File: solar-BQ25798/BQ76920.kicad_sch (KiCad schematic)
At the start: 33 parts, among them Q1801 CSD17581Q3A, Q1802 CSD17581Q3A, Q1803 Q_PMOS_GSD, U2 BQ76920PW

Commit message: BQ25798 WIP
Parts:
- Q1801: renamed from Q1802; value CSD17581Q3A -> CSD17578Q3A; symbol Transistor_FET:CSD17581Q3A -> cacophony-library:CSD17578Q3A; LCSC Part C2866708 -> C205986
- Q1803: renamed from Q1801; value CSD17581Q3A -> CSD17578Q3A; symbol Transistor_FET:CSD17581Q3A -> cacophony-library:CSD17578Q3A; LCSC Part C2866708 -> C205986
- renumbered C6 to C1801, C1803 to C1802, C3 to C1803, C2 to C1804, C1 to C1805, C4 to C1806, C5 to C1807, C1801 to C1808, C1802 to C1809, C7 to C1810, C8 to C1811, C10 to C1812, C9 to C1813, D1802 to D1801, Q1803 to Q1802, R6 to R1801, R5 to R1802, R4 to R1803, R3 to R1804, R2 to R1805, R1 to R1806, R1801 to R1807, R211 to R1808, R1802 to R1809, R1803 to R1810, R7 to R1811, R1805 to R1812, R1804 to R1813, R9 to R1814, U2 to U1801

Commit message: Solar battery WIP
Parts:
- U1801: footprint cacophony-library:TSSOP-20_4.4x6.5mm_P0.65mm -> Package_SO:TSSOP-20_4.4x6.5mm_P0.65mm
- renumbered C1803 to C1801, C1810 to C1802, C1804 to C1803, C1805 to C1804, C1806 to C1805, C1813 to C1806, C1812 to C1807, C1807 to C1808, C1811 to C1809, C1801 to C1810, C1802 to C1811, C1808 to C1812, C1809 to C1813, Q1802 to Q1801, Q1801 to Q1802, R1811 to R1801, R1801 to R1802, R1802 to R1803, R1803 to R1804, R1804 to R1805, R1814 to R1806, R1805 to R1807, R1806 to R1808, R1812 to R1809, R1807 to R1810, R1809 to R1811, R1810 to R1812, R1808 to R1814
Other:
- moved on the sheet: C1801, C1802, C1803, C1804, C1805, C1806, C1807, C1808, C1809, C1810, C1811, C1812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

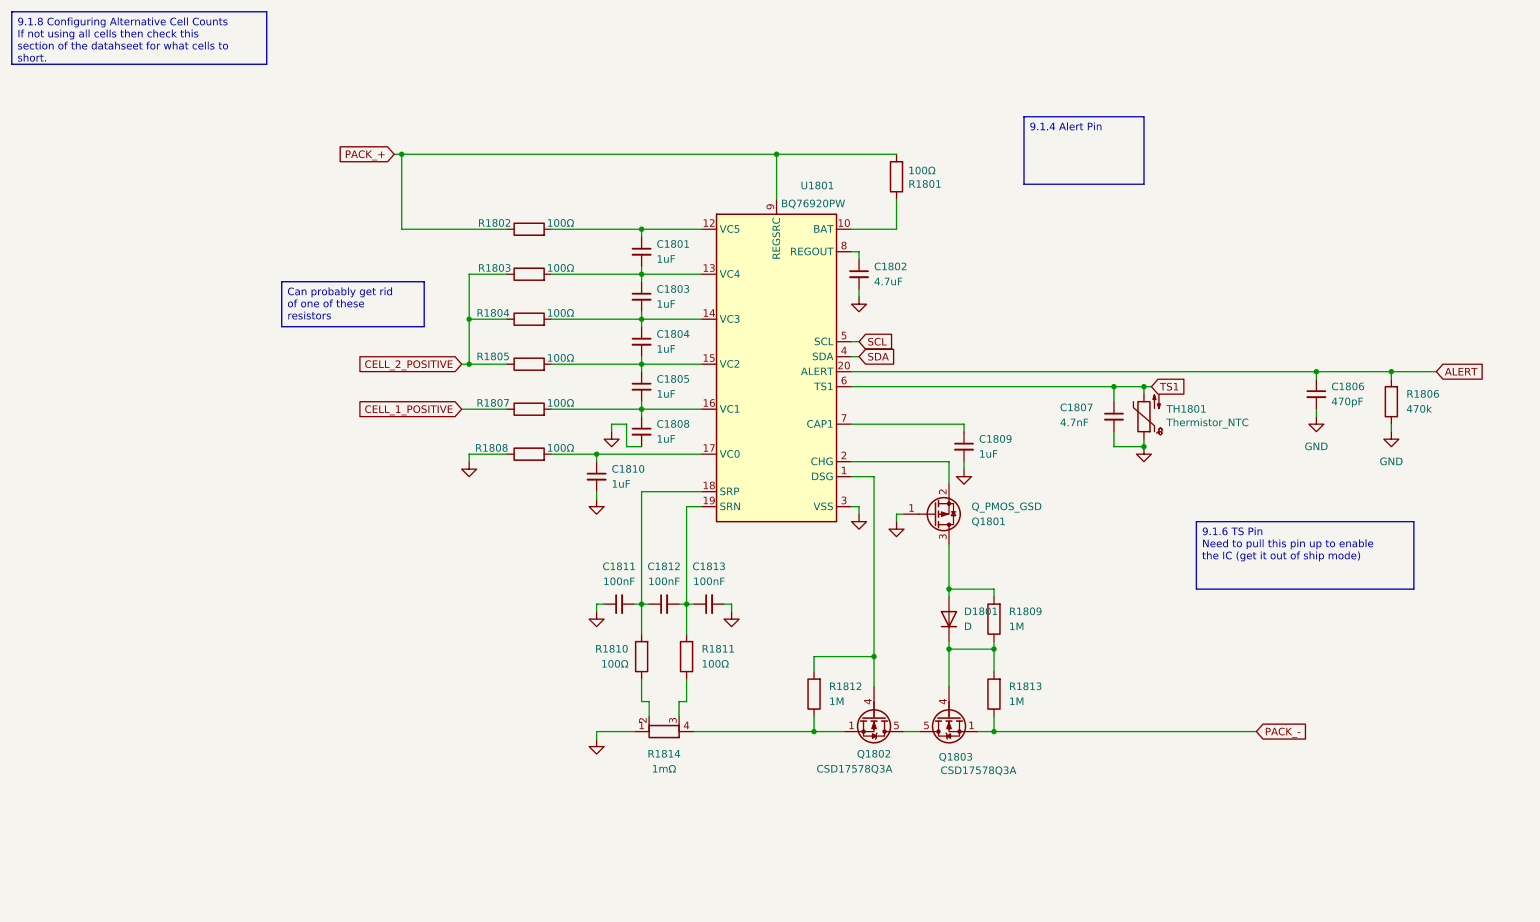
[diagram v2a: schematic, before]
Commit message: Update battery PCB
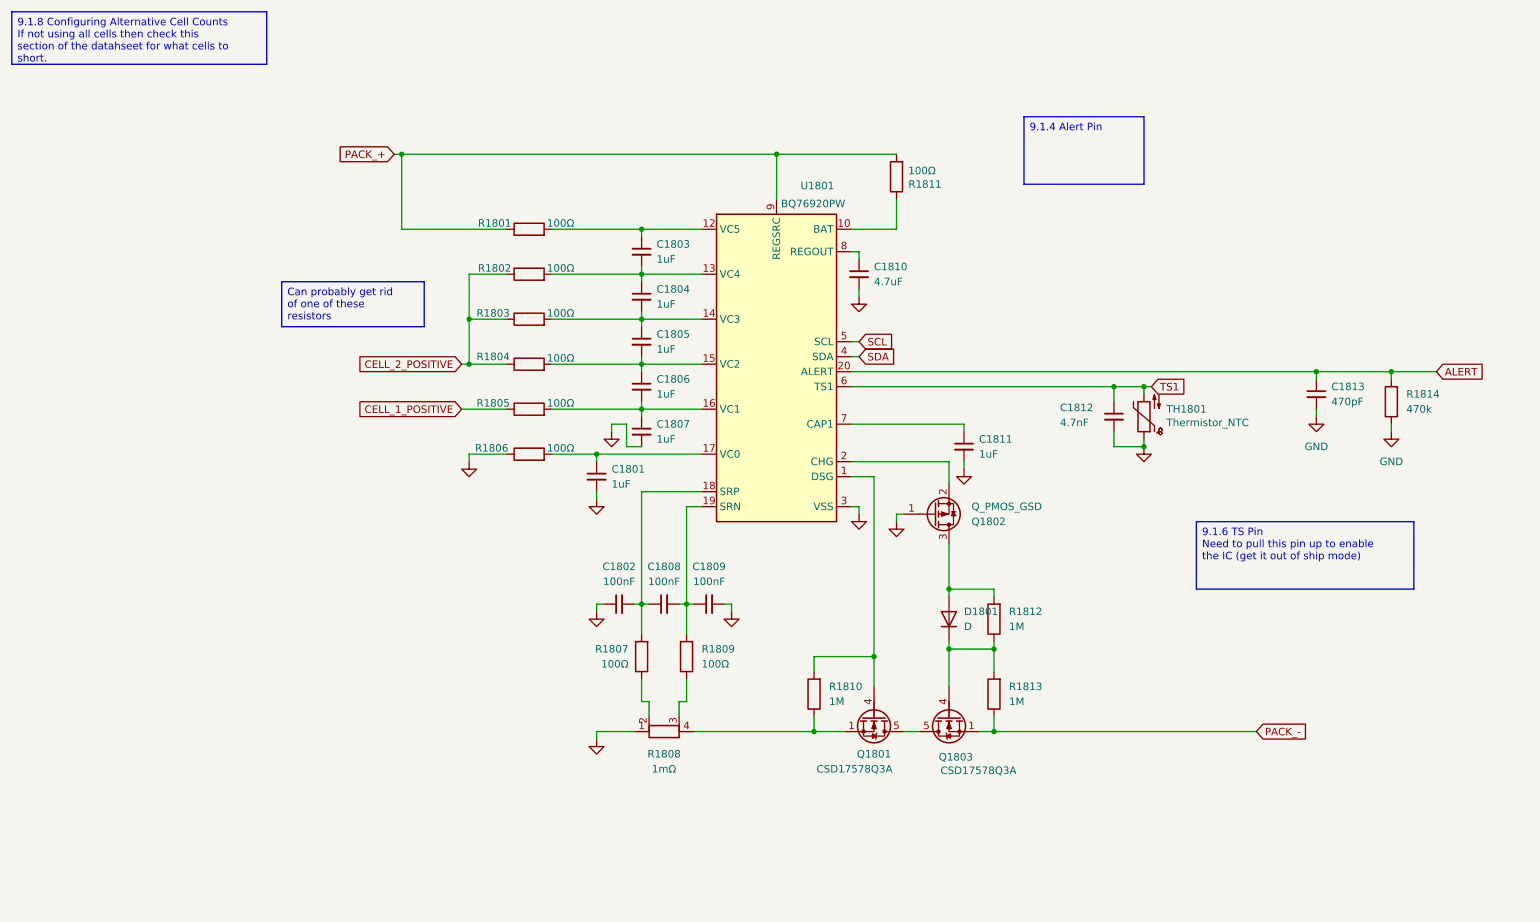
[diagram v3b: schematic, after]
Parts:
- renumbered C1810 to C1801, C1811 to C1802, C1801 to C1803, C1803 to C1804, C1804 to C1805, C1805 to C1806, C1808 to C1807, C1812 to C1808, C1813 to C1809, C1802 to C1810, C1809 to C1811, C1807 to C1812, C1806 to C1813, Q1802 to Q1801, Q1801 to Q1802, R1802 to R1801, R1803 to R1802, R1804 to R1803, R1805 to R1804, R1807 to R1805, R1808 to R1806, R1810 to R1807, R1814 to R1808, R1811 to R1809, R1812 to R1810, R1801 to R1811, R1809 to R1812, R1806 to R1814

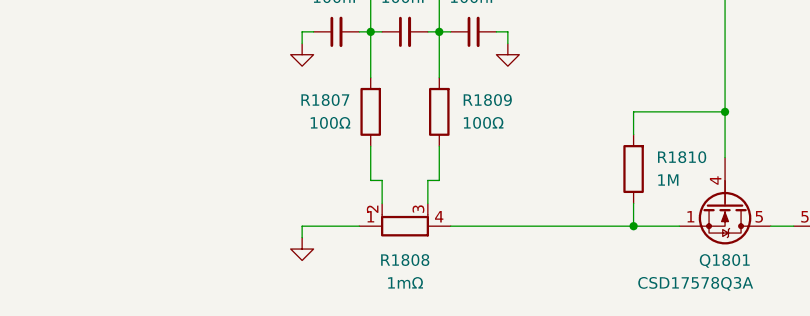
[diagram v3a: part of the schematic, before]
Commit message: Update shunt resistor
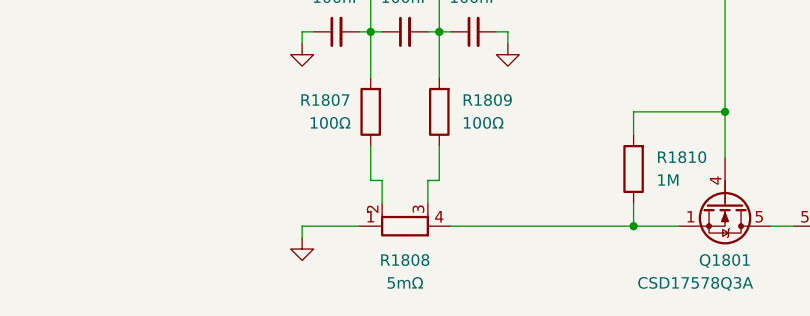
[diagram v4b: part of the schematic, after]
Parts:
- R1808: value 1mΩ -> 5mΩ; LCSC Part C7467246 -> C2988648
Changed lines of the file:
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@@
 			)
 		)
-		(property "Value" "1mΩ"
+		(property "Value" "5mΩ"
 			(at 130.81 152.4 90)
 			(effects
@@
 			)
 		)
-		(property "LCSC Part" "C7467246"
+		(property "LCSC Part" "C2988648"
 			(at 130.81 146.05 90)
 			(effects

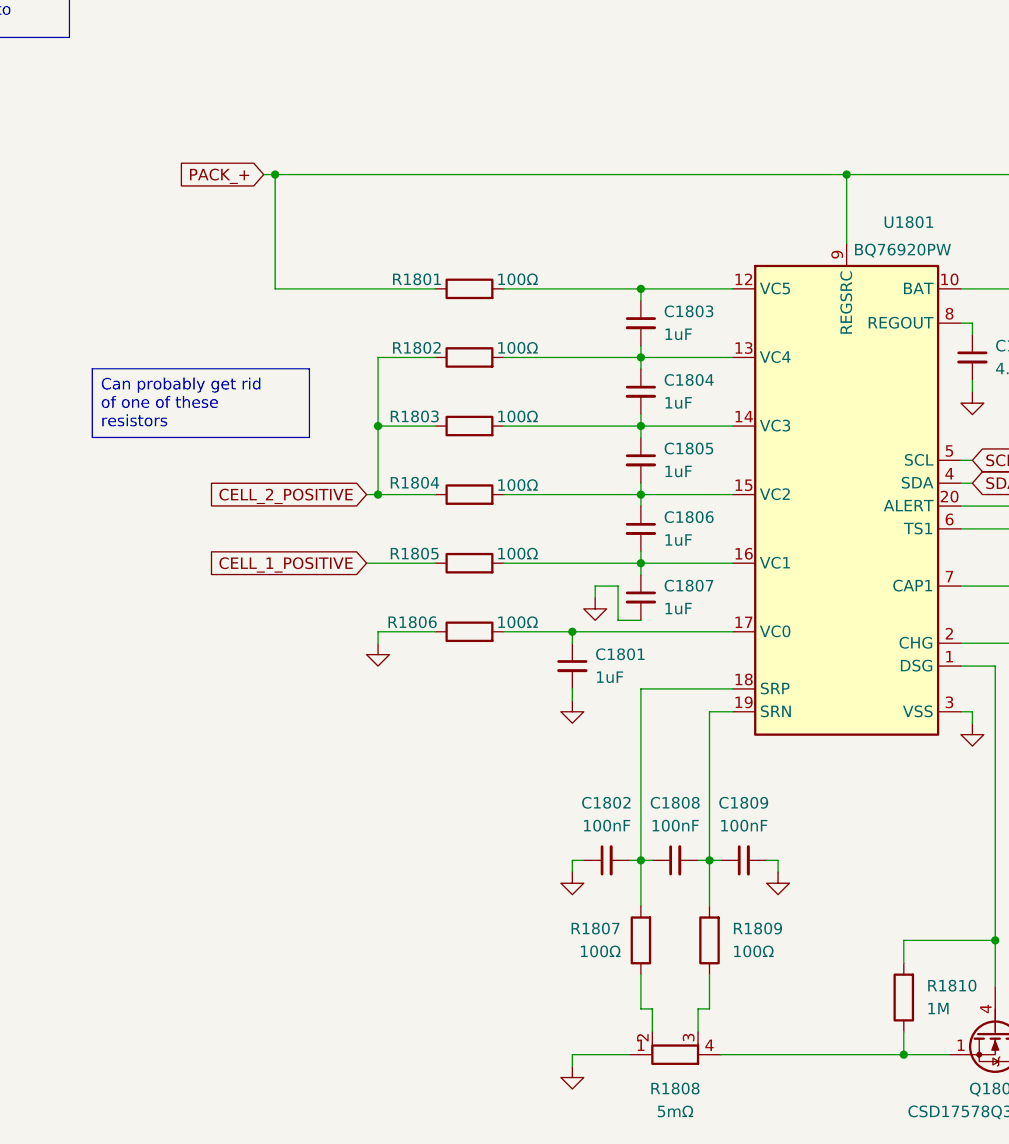
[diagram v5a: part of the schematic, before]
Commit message: Fix pin for serial out and other small fixes
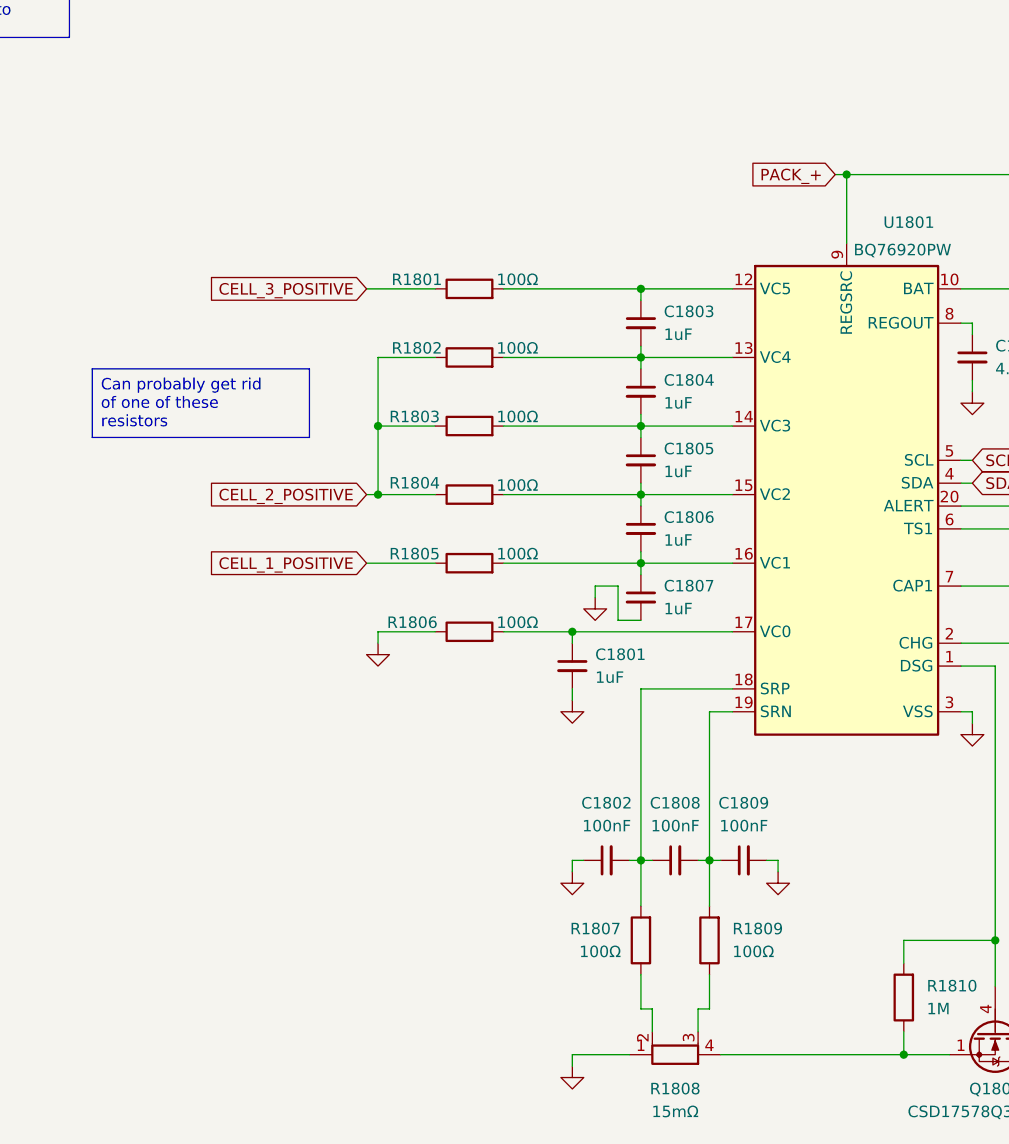
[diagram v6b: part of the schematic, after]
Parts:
- R1808: value 5mΩ -> 15mΩ; LCSC Part C2988648 -> C875667
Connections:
- net PACK_+: no longer R1801.1
- new net CELL_3_POSITIVE: R1801.1
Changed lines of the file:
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@@
 	)
 	(junction
-		(at 86.36 48.26)
-		(diameter 0)
-		(color 0 0 0 0)
-	)
-	(junction
 		(at 156.21 146.05)
 		(diameter 0)
@@
 	)
 	(junction
-		(at 149.86 48.26)
+		(at 186.69 146.05)
 		(diameter 0)
 		(color 0 0 0 0)
 	)
 	(junction
-		(at 186.69 146.05)
+		(at 179.07 132.08)
 		(diameter 0)
 		(color 0 0 0 0)
 	)
 	(junction
-		(at 179.07 132.08)
+		(at 127 124.46)
 		(diameter 0)
 		(color 0 0 0 0)
 	)
 	(junction
-		(at 127 124.46)
+		(at 149.86 48.26)
 		(diameter 0)
 		(color 0 0 0 0)
@@
 	(wire
 		(pts
-			(xy 86.36 48.26) (xy 86.36 60.96)
-		)
-		(stroke
-			(width 0)
-			(type default)
-		)
-	)
-	(wire
-		(pts
 			(xy 111.76 68.58) (xy 127 68.58)
 		)
@@
 	(wire
 		(pts
-			(xy 86.36 60.96) (xy 104.14 60.96)
+			(xy 96.52 60.96) (xy 104.14 60.96)
 		)
 		(stroke
@@
 	(wire
 		(pts
-			(xy 85.09 48.26) (xy 86.36 48.26)
-		)
-		(stroke
-			(width 0)
-			(type default)
-		)
-	)
-	(wire
-		(pts
 			(xy 134.62 140.97) (xy 133.35 140.97)
 		)
@@
 	(wire
 		(pts
-			(xy 149.86 48.26) (xy 86.36 48.26)
+			(xy 148.59 48.26) (xy 149.86 48.26)
 		)
 		(stroke
@@
 		)
 	)
+	(global_label "CELL_3_POSITIVE"
+		(shape input)
+		(at 96.52 60.96 180)
+		(fields_autoplaced yes)
+		(effects
+			(font
+				(size 1.27 1.27)
+			)
+			(justify right)
+		)
+		(property "Intersheetrefs" "${INTERSHEET_REFS}"
+			(at 77.6901 60.96 0)
+			(hide yes)
+			(show_name no)
+			(do_not_autoplace no)
+			(effects
+				(font
+					(size 1.27 1.27)
+				)
+				(justify right)
+			)
+		)
+	)
 	(global_label "PACK_+"
 		(shape input)
-		(at 85.09 48.26 180)
+		(at 148.59 48.26 180)
 		(fields_autoplaced yes)
 		(effects
@@
 		)
 		(property "Intersheetrefs" "${INTERSHEET_REFS}"
-			(at 74.6662 48.26 0)
+			(at 138.1662 48.26 0)
 			(hide yes)
 			(show_name no)
@@
 			)
 		)
-		(property "Value" "5mΩ"
+		(property "Value" "15mΩ"
 			(at 130.81 152.4 90)
 			(show_name no)
@@
 			)
 		)
-		(property "LCSC Part" "C2988648"
+		(property "LCSC Part" "C875667"
 			(at 130.81 146.05 90)
 			(hide yes)

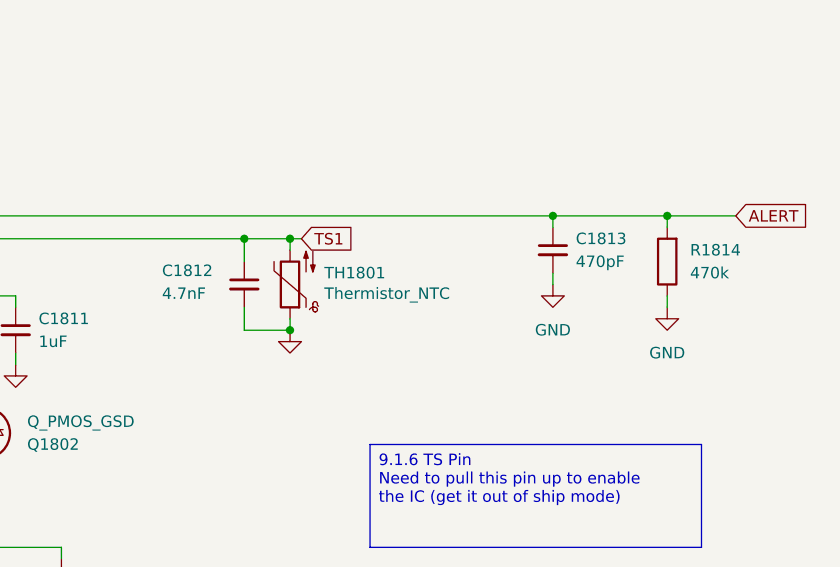
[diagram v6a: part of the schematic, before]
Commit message: Reduce number of different resistor and capacitor values
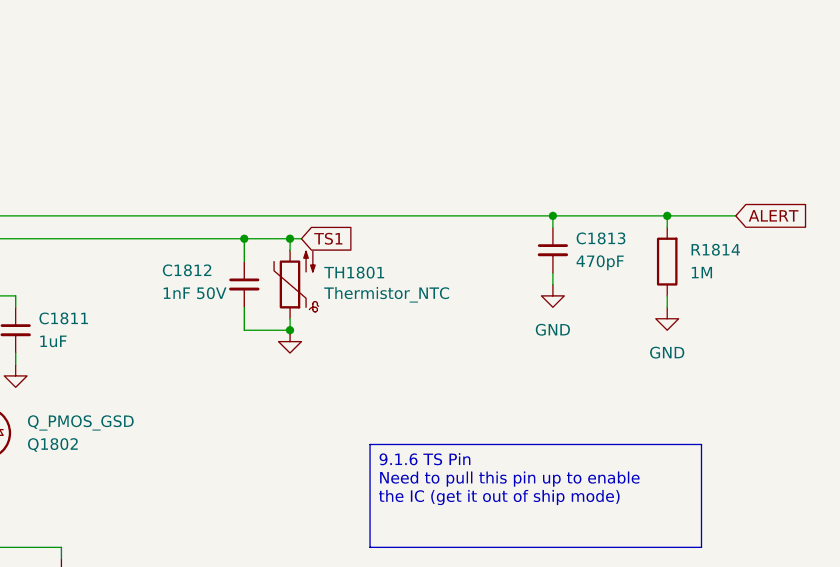
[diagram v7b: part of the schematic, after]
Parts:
- C1802, C1808, C1809: LCSC Part C307331 -> C1525
- C1812: value 4.7nF -> 1nF 50V; LCSC Part C1538 -> C1523
- R1814: value 470k -> 1M; LCSC Part C25790 -> C26083
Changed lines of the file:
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@@
 			)
 		)
-		(property "LCSC Part" "C307331"
+		(property "LCSC Part" "C1525"
 			(at 138.43 124.46 90)
 			(hide yes)
@@
 			)
 		)
-		(property "LCSC Part" "C307331"
+		(property "LCSC Part" "C1525"
 			(at 130.81 124.46 90)
 			(hide yes)
@@
 			)
 		)
-		(property "Value" "4.7nF"
+		(property "Value" "1nF 50V"
 			(at 197.866 93.726 0)
 			(show_name no)
@@
 			)
 		)
-		(property "LCSC Part" "C1538"
+		(property "LCSC Part" "C1523"
 			(at 207.01 92.71 0)
 			(hide yes)
@@
 			)
 		)
-		(property "LCSC Part" "C307331"
+		(property "LCSC Part" "C1525"
 			(at 123.19 124.46 90)
 			(hide yes)
@@
 			)
 		)
-		(property "Value" "470k"
+		(property "Value" "1M"
 			(at 256.54 91.4399 0)
 			(show_name no)
@@
 			)
 		)
-		(property "LCSC Part" "C25790"
+		(property "LCSC Part" "C26083"
 			(at 254 90.17 0)
 			(hide yes)
